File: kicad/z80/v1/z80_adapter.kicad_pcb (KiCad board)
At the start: 2 copper layers, 49 x 75.2 mm, 45 parts, among them P1 Conn_02x20_Odd_Even, P2 Conn_02x20_Odd_Even, P3 Conn_01x03, SW1 SW_Push, SW2 SW_Push, U1 Z80CPU, U2 74LVC4245, U3 74LVC4245, U4 74LVC4245, U5 74LVC4245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

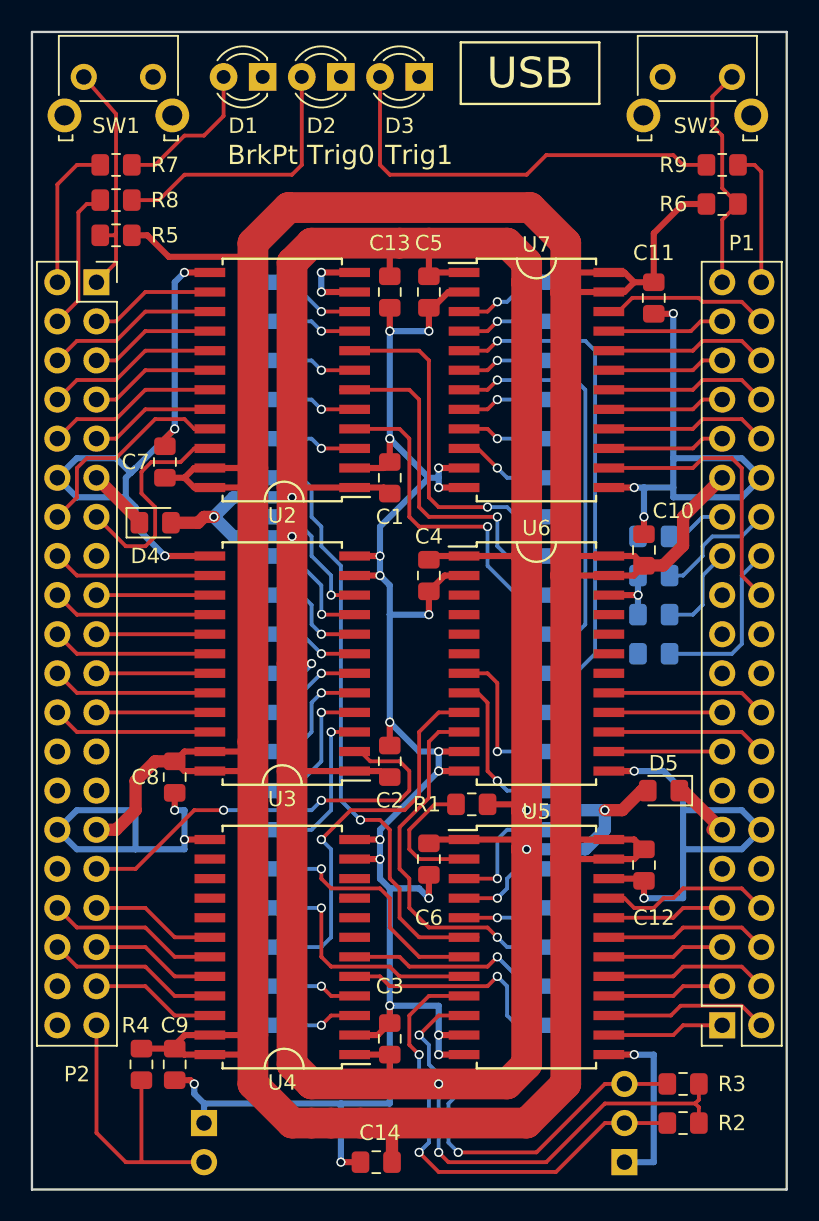
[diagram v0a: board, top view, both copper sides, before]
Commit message: Kicad z80: added clock filtering
Change-Id: Iffb927aec6c569c380b294d3bcf015d7ca117871
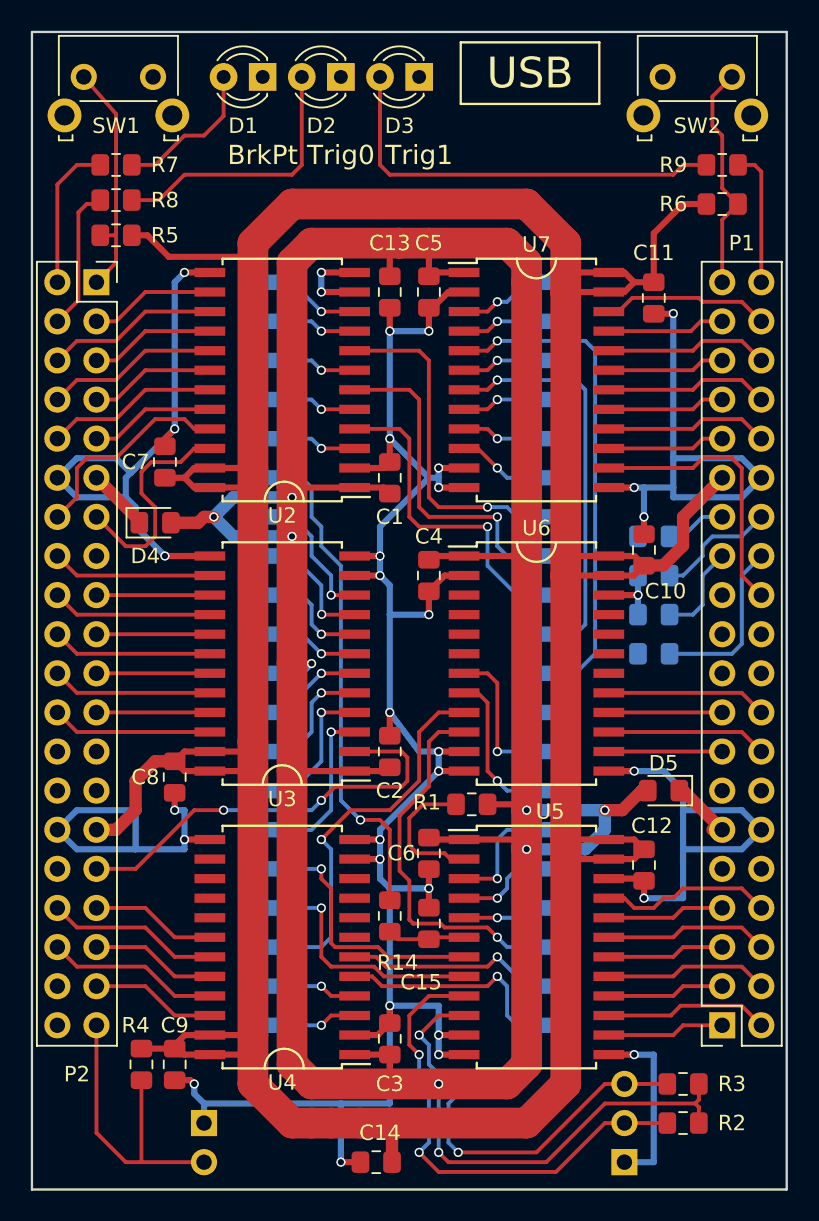
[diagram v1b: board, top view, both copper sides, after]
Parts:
- added C15: 0pF, Capacitor_SMD:C_0805_2012Metric_Pad1.15x1.40mm_HandSolder, F.Cu at (194.3, 107.7)
- added R14: 0, Resistor_SMD:R_0805_2012Metric_Pad1.15x1.40mm_HandSolder, F.Cu at (191.8, 107.2)
- moved C2 0.64 mm to (191.8, 96.5)
- moved C6 0.37 mm to (194.3, 103.1)
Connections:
- U5 pad 6: /CLK -> /FILTERED_CLK
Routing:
- net /FILTERED_CLK: track 0.00 -> 6.55 mm
- net /CLK: track 38.2 -> 31.9 mm
- net /INT: track 15.0 -> 16.0 mm
- net /HALT: track 24.5 -> 24.0 mm
- net Net-(D3-Pad2): track 28.0 -> 27.4 mm

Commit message: Kicad z80: add more power vias
Change-Id: If1bc8cabde72e3d8b67fdd21e4c5b55accf4307d
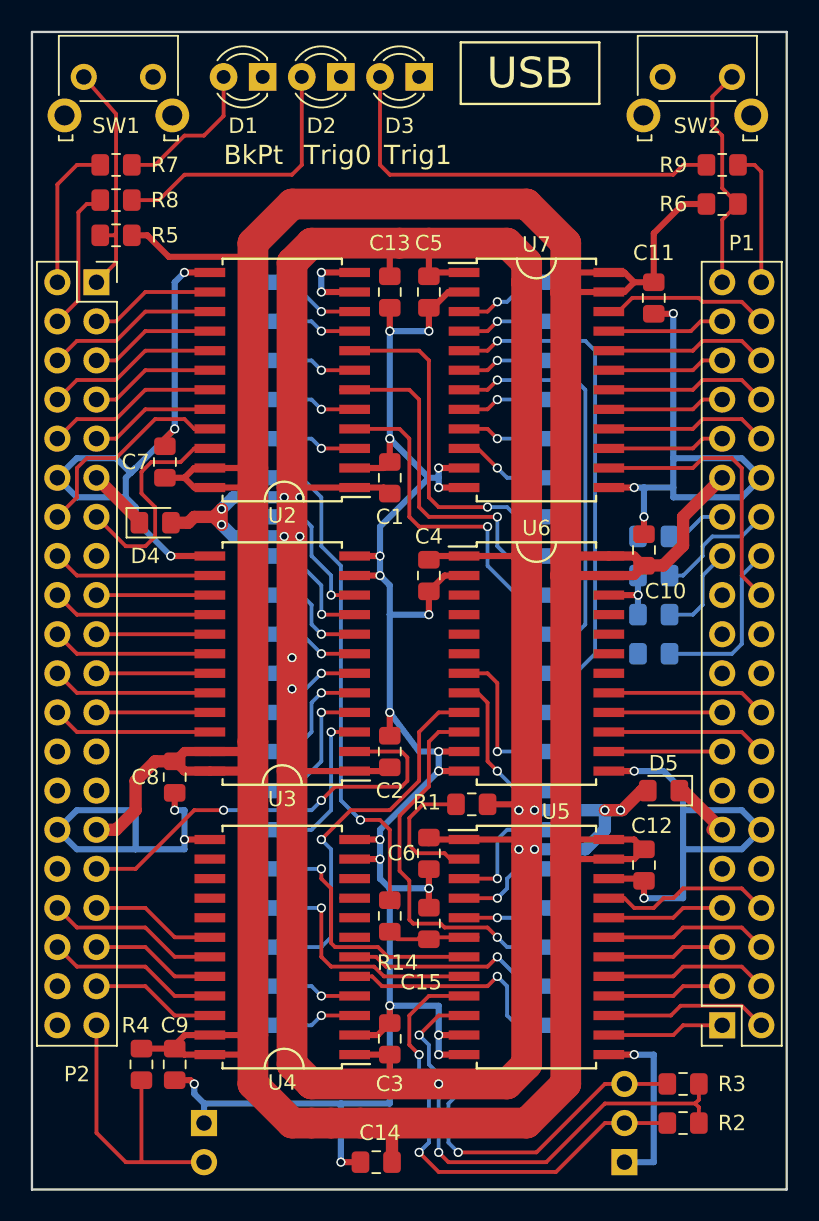
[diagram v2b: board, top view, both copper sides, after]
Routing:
- net /5V: track 235.3 -> 238.6 mm, vias 9 -> 16
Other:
- board text added: "BkPt"
- board text removed: "BrkPt"

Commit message: Kicad z80: change via sizes
Change-Id: I87a36dab22496e9229797047826a10f0319e28f1
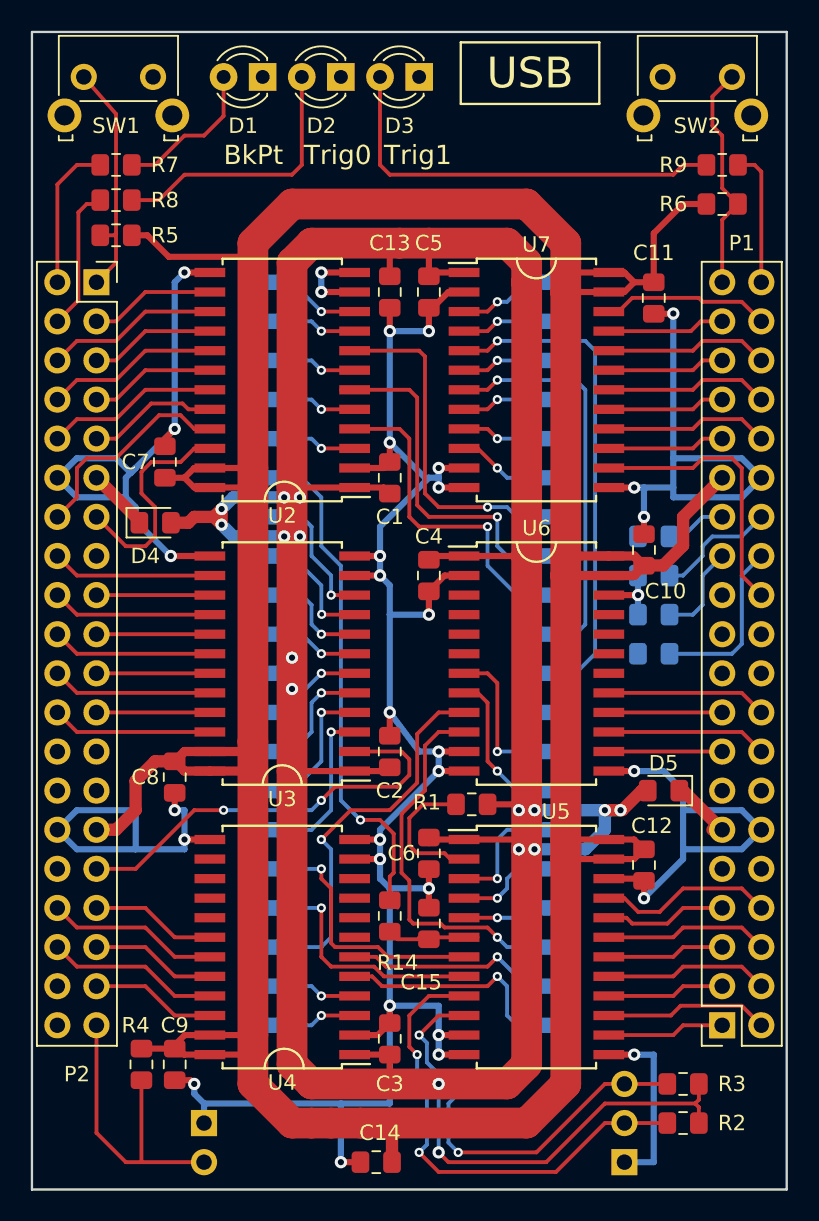
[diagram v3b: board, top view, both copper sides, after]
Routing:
- net /GND: track 276.4 -> 274.8 mm
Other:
- net class Default: via_drill 0.4 -> 0.3
- net class Power: via_dia 0.6 -> 0.8
- rule via_min_size: 0.4 -> 0.6
